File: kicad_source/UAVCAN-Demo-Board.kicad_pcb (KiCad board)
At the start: 2 copper layers, 21 x 25 mm, 18 parts, among them CN1 CONN_01X05, CN2 691322310004, CN3 GH_SM04B-GHS-TB, CN4 GH_SM04B-GHS-TB, U1 TCAN332GDR

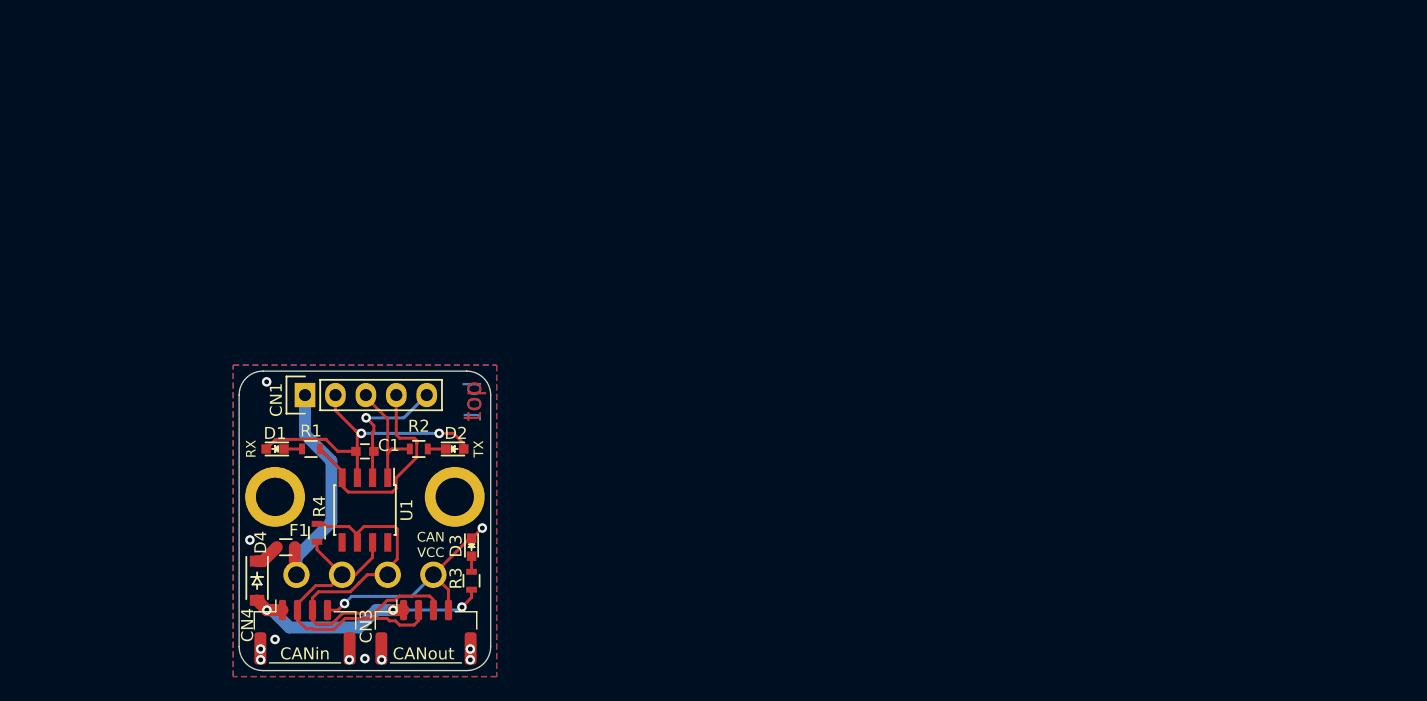
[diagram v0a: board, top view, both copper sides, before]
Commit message: started layout, added THT parts
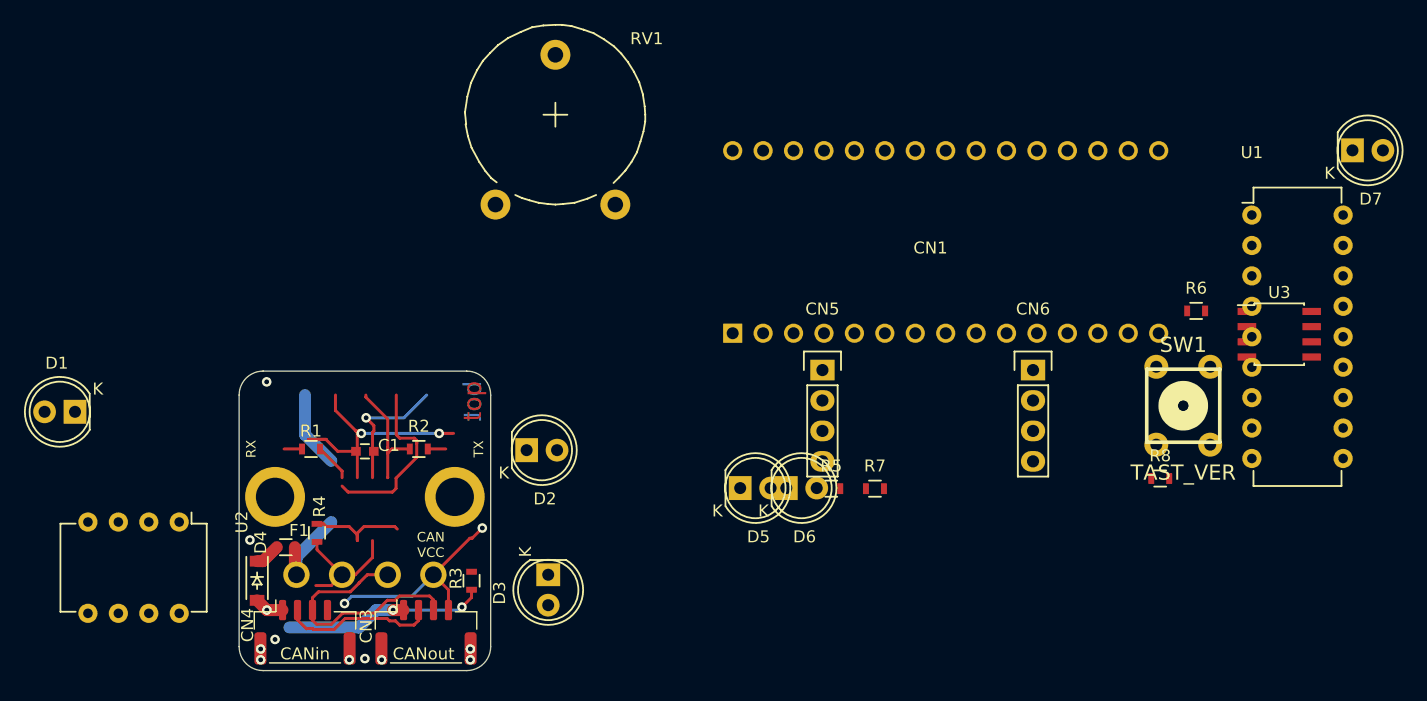
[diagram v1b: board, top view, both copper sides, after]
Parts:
- added CN5: 691322310004, pin_headers:Pin_Header_Straight_1x04, F.Cu at (186.2, 91.4)
- added CN6: 691322310004, pin_headers:Pin_Header_Straight_1x04, F.Cu at (203.8, 91.4)
- added D5: 150060YS75000, LEDs:LED-5MM, F.Cu at (179.3, 101.3)
- added D6: 150060YS75000, LEDs:LED-5MM, F.Cu at (183.2, 101.3)
- added D7: 150060YS75000, LEDs:LED-5MM, F.Cu at (230.4, 73.1)
- added R5: 1k, resistors:R_0603, F.Cu at (186.9, 101.3)
- added R6: 1k, resistors:R_0603, F.Cu at (217.4, 86.5)
- added R7: 1k, resistors:R_0603, F.Cu at (190.6, 101.3)
- added R8: 10k, resistors:R_0603, F.Cu at (214.4, 100.5)
- added RV1: POT, potentiometers:Potentiometer_Trimmer-Piher_PT15-V12-5_horizontal, F.Cu at (158.9, 77.6)
- added SW1: TAST_VER, mechanical-switches:PCB_PUSH, F.Cu at (216.3, 94.4)
- added U2: SN65VHD232, DIP:DIP-8_W7.62mm, F.Cu at (132.5, 104.1)
- added U3: DS18B20, SOIC:SOIC-8_3.9x4.9mm_Pitch1.27mm, F.Cu at (224.3, 88.4)
- CN1: value CONN_01X05 -> ARDUINO_NANO_33; footprint pin_headers:Pin_Header_Straight_1x05 -> MODULE_compute:ARDUINO_NANO_33
- D1, D2, D3: footprint LEDs:LED_0603 -> LEDs:LED-5MM
- U1: value TCAN332GDR -> MCP2515; footprint SOIC:SOIC-8_3.9x4.9mm_Pitch1.27mm -> DIP:DIP-18_W7.62mm
- moved U1 78.0 mm to (222.0, 78.5), turned to 0 degrees
- moved CN1 55.0 mm to (196.5, 80.7), turned to 0 degrees
- moved D1 17.0 mm to (123.8, 94.9)
- moved D3 6.80 mm to (163.3, 108.5)
- moved D2 6.00 mm to (161.5, 98.1)
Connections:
- CN1 pad 1: +5V -> /SPI_SCK
- CN1 pad 3: /CAN_TX -> (no net)
- CN1 pad 4: /CAN_RX -> /ANALOG
- CN1 pad 5: GND -> (no net)
- U1 pad 2: GND -> /CAN_RX
- U1 pad 3: +3V3 -> (no net)
- U1 pad 4: /CAN_RX -> (no net)
- U1 pad 6: /CANL -> (no net)
- U1 pad 7: /CANH -> (no net)
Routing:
- net +3V3: track 27.5 -> 22.0 mm
- net +5V: track 19.5 -> 14.4 mm
- net /CANL: track 33.8 -> 30.2 mm
- net /CANH: track 26.3 -> 23.6 mm
- net /CANVCC: track 22.7 -> 20.2 mm
- net GND: track 30.6 -> 28.9 mm
- net Net-(D3-Pad2): track 1.30 -> 0.00 mm
- removed copper zone on B.Cu, net GND
- removed copper zone on F.Cu, net GND
